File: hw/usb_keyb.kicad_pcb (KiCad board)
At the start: 2 copper layers, 99.1 x 48.3 mm, 73 parts, among them J1 POWER, J10 SPI, J12 ID, J13 ID, J2 Micro_SD_Card, J3 USB_1, J4 USB_2, J5 MX_ROW, J6 MX_COL, J7 I2C, J8 UART, J9 PROG, SW1 RESET, U1 LM3671MF, U2 STM32F407VETx, U3 STMPS2141STR, U4 STMPS2141STR, U5 74ALVC164245, U6 74ALVC164245, U7 74ALVC164245, Y1 8MHz

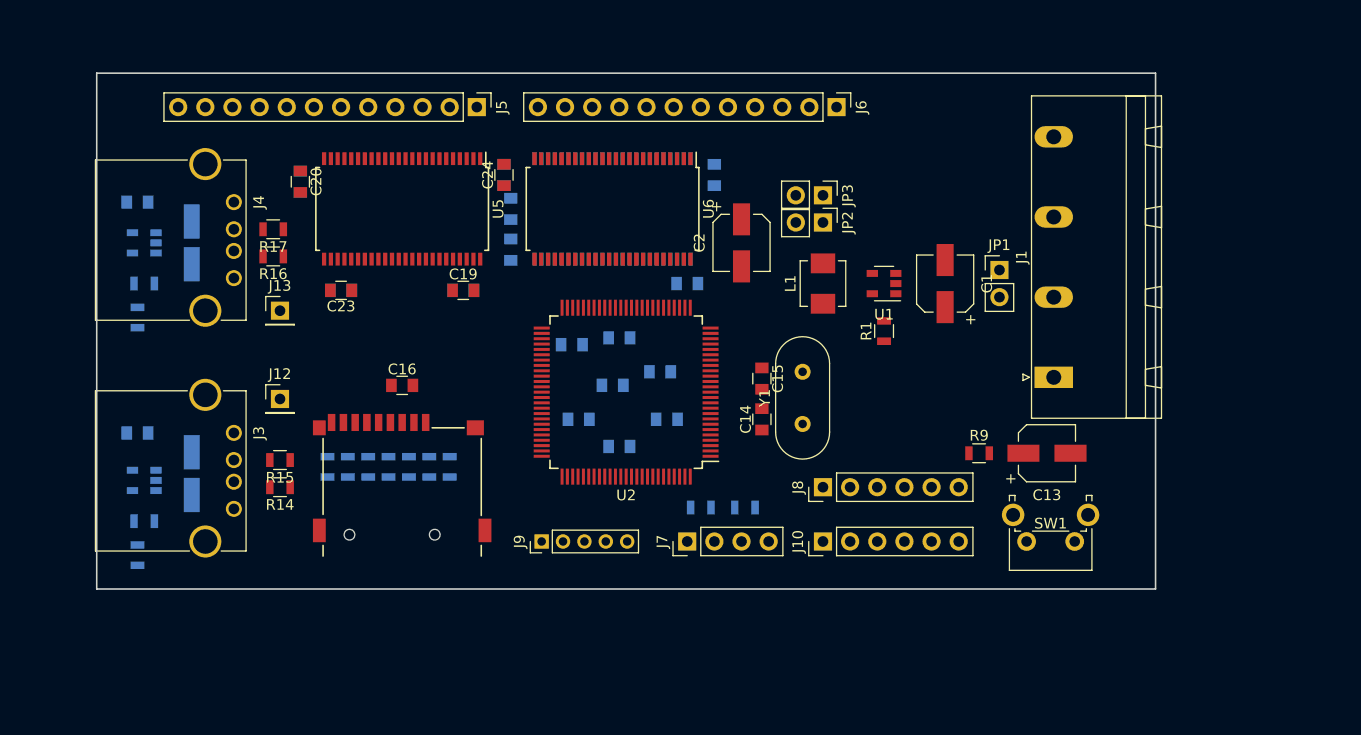
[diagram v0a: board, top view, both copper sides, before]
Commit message: Изменён разъём ZX-BUS, обновлена компоновка
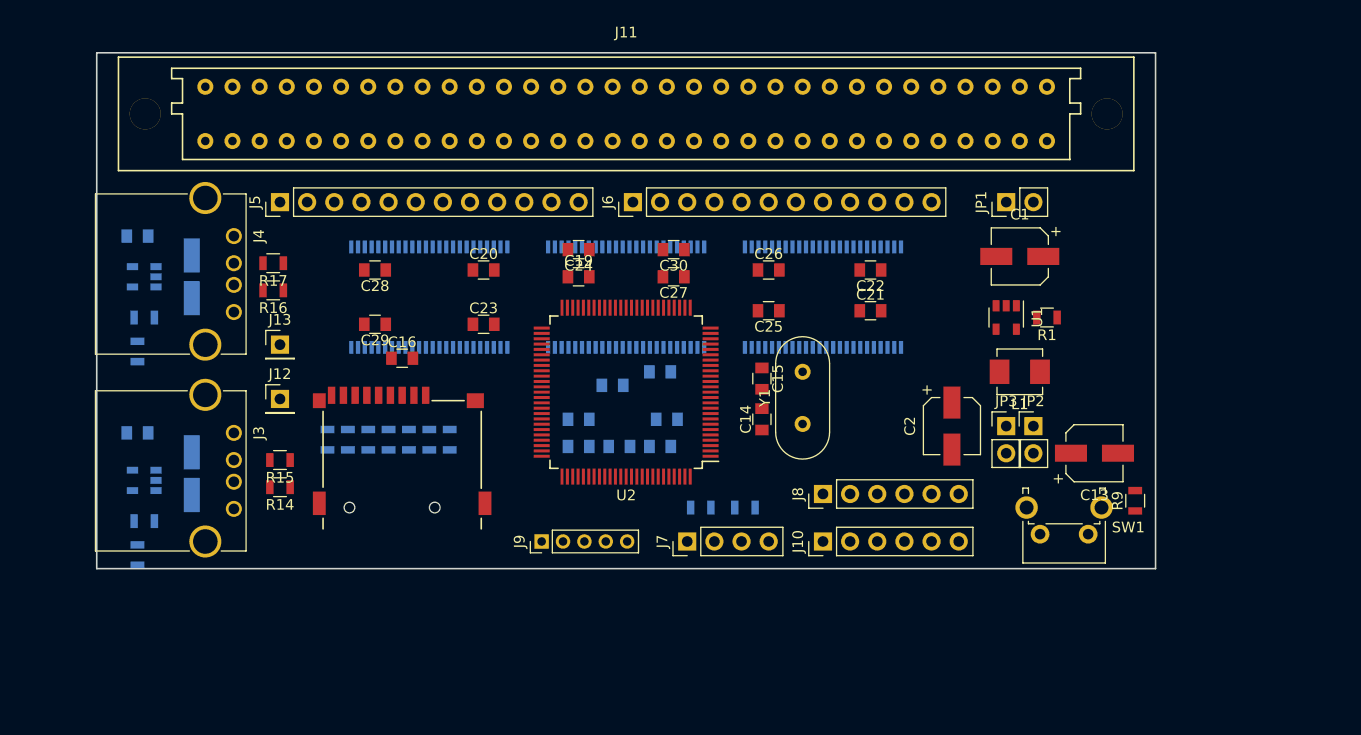
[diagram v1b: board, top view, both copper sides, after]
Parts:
- removed J1: POWER, Connectors_Phoenix:PhoenixContact_GMSTBA-G_04x7.50mm_Angled
- added J11: ZX-BUS, Connectors_IEC_DIN:Socket_DIN41612-CaseC1-AC-Female-64Pin-2rows, F.Cu at (146.1, 66.0)
- C21, C22, C25, C26, C27, C28, C29, C30: moved to F.Cu
- U5, U6: moved to B.Cu
- moved JP3 27.6 mm to (181.6, 95.2), turned to 0 degrees
- moved JP2 27.4 mm to (184.2, 95.2), turned to 0 degrees
- moved C2 26.1 mm to (176.5, 95.2)
- moved C25 24.8 mm to (159.4, 84.5), turned to 180 degrees
- moved C26 24.8 mm to (159.4, 80.6), turned to 0 degrees
- moved U6 21.3 mm to (164.5, 83.2)
- moved J6 21.0 mm to (146.7, 74.3), turned to 90 degrees
- moved J5 20.4 mm to (113.7, 74.3), turned to 90 degrees
- moved L1 20.2 mm to (182.9, 90.2), turned to 180 degrees
- moved C27 19.7 mm to (150.5, 81.3)
- moved C20 19.0 mm to (132.7, 80.6), turned to 0 degrees
- moved C30 17.3 mm to (150.5, 78.7), turned to 180 degrees
- moved C21 17.3 mm to (168.9, 84.5)
- moved C22 17.1 mm to (168.9, 80.6), turned to 180 degrees
- moved R1 15.3 mm to (185.4, 85.1), turned to 180 degrees
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
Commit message: Убраны буферные элементы, все внешние сигналы будут Open Drain
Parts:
- removed C19, C20, C21, C22, C23, C24, C25, C26, C27, C28, C29, C30: 100n, Capacitors_SMD:C_0805
- removed U5, U6, U7: 74ALVC164245, Housings_SSOP:SSOP-48_7.5x15.9mm_Pitch0.635mm
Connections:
- net DR4 renamed Net-(U2-Pad90)
- net DR5 renamed Net-(U2-Pad91)
- net DR6 renamed Net-(U2-Pad95)
- net DR7 renamed Net-(U2-Pad96)
- J2 pad 1: D2 -> D3
- J2 pad 2: D3 -> CMD
- J2 pad 3: CMD -> +3V3
- J2 pad 4: +3V3 -> CK
- J2 pad 5: CK -> GND
- J2 pad 6: GND -> D0
- J2 pad 7: D0 -> D1
- J2 pad 8: D1 -> CD
- J2 pad 9: CD -> Net-(J2-Pad9)
- U2 pad 1: O2 -> ZD2
- U2 pad 15: I0 -> ZA8
- U2 pad 16: I1 -> ZA9
- U2 pad 17: I2 -> ZA10
- U2 pad 18: I3 -> ZA11
- U2 pad 2: O3 -> ZD3
- U2 pad 23: INT0 -> ZIORQn
- U2 pad 24: INT1 -> ZRDn
- U2 pad 25: INT2 -> ZWRn
- U2 pad 26: INT3 -> ZMREQn
- U2 pad 3: O4 -> ZD4
- U2 pad 33: I4 -> ZA12
- U2 pad 34: I5 -> ZA13
- U2 pad 35: DR0 -> Net-(U2-Pad35)
- U2 pad 36: DR1 -> Net-(U2-Pad36)
- U2 pad 37: DR2 -> Net-(U2-Pad37)
- U2 pad 38: O7 -> ZD7
- U2 pad 39: O8 -> MC8
- U2 pad 4: O5 -> ZD5
- U2 pad 40: O9 -> MC9
- U2 pad 41: O10 -> MC10
- U2 pad 42: O11 -> MC11
- U2 pad 43: M1n -> ZM1n
- U2 pad 44: INTn -> ZINTn
- U2 pad 45: NMIn -> ZNMIn
- U2 pad 5: O6 -> ZD6
- U2 pad 55: A5 -> ZA5
- U2 pad 56: A6 -> ZA6
- U2 pad 57: A7 -> ZA7
- U2 pad 60: I10 -> MR10
- U2 pad 61: I11 -> MR11
- U2 pad 63: I6 -> ZA14
- U2 pad 64: I7 -> ZA15
- U2 pad 81: I8 -> MR8
- U2 pad 82: I9 -> MR9
- U2 pad 84: A0 -> ZA0
- U2 pad 85: A1 -> ZA1
- U2 pad 86: A2 -> ZA2
- U2 pad 87: A3 -> ZA3
- U2 pad 88: A4 -> ZA4
- U2 pad 89: DR3 -> Net-(U2-Pad89)
- U2 pad 97: O0 -> ZD0
- U2 pad 98: O1 -> ZD1

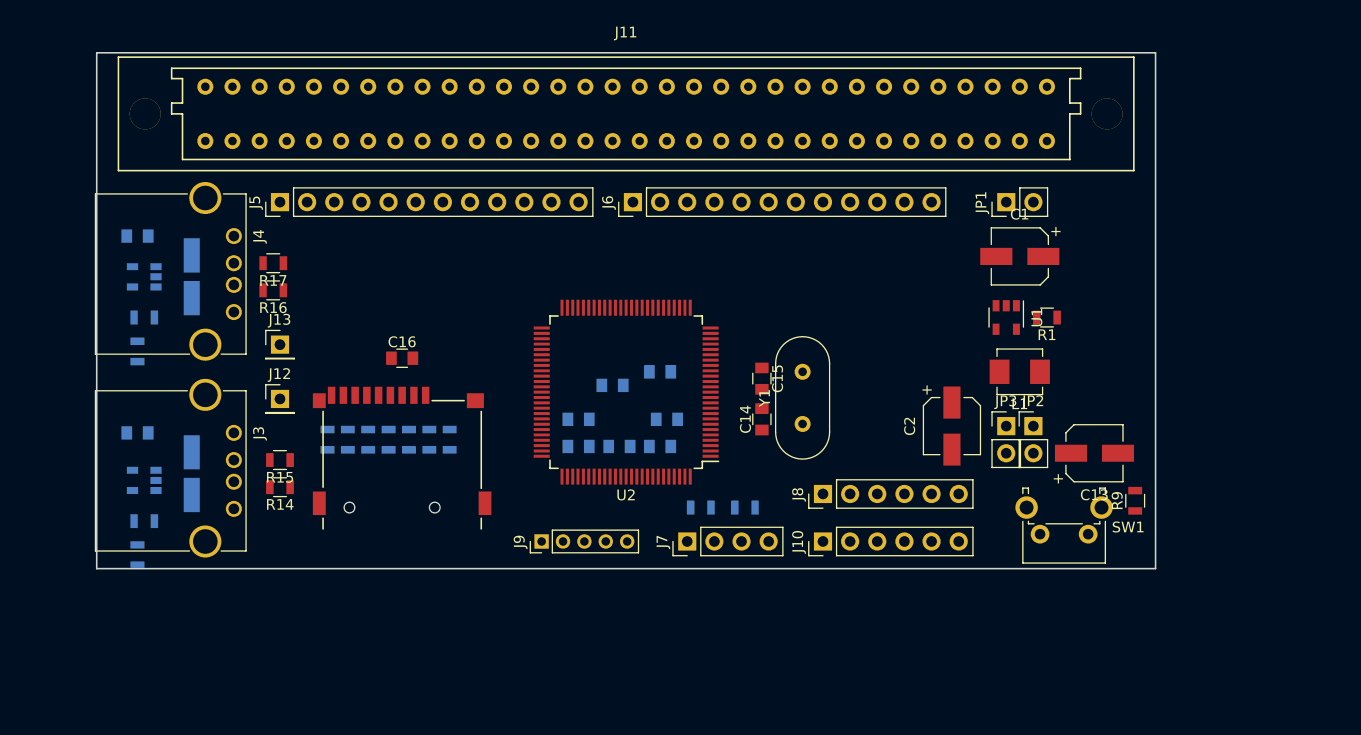
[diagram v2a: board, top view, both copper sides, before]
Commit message: Множественные изменения в схеме:
1) Заменён разъём USB на сдвоенный;
2) Добавлен Ethernet-PHY;
3) Изменено назначение служебных сигналов USB и интерфейсов;
4) внешние шины временно отключены от МК.
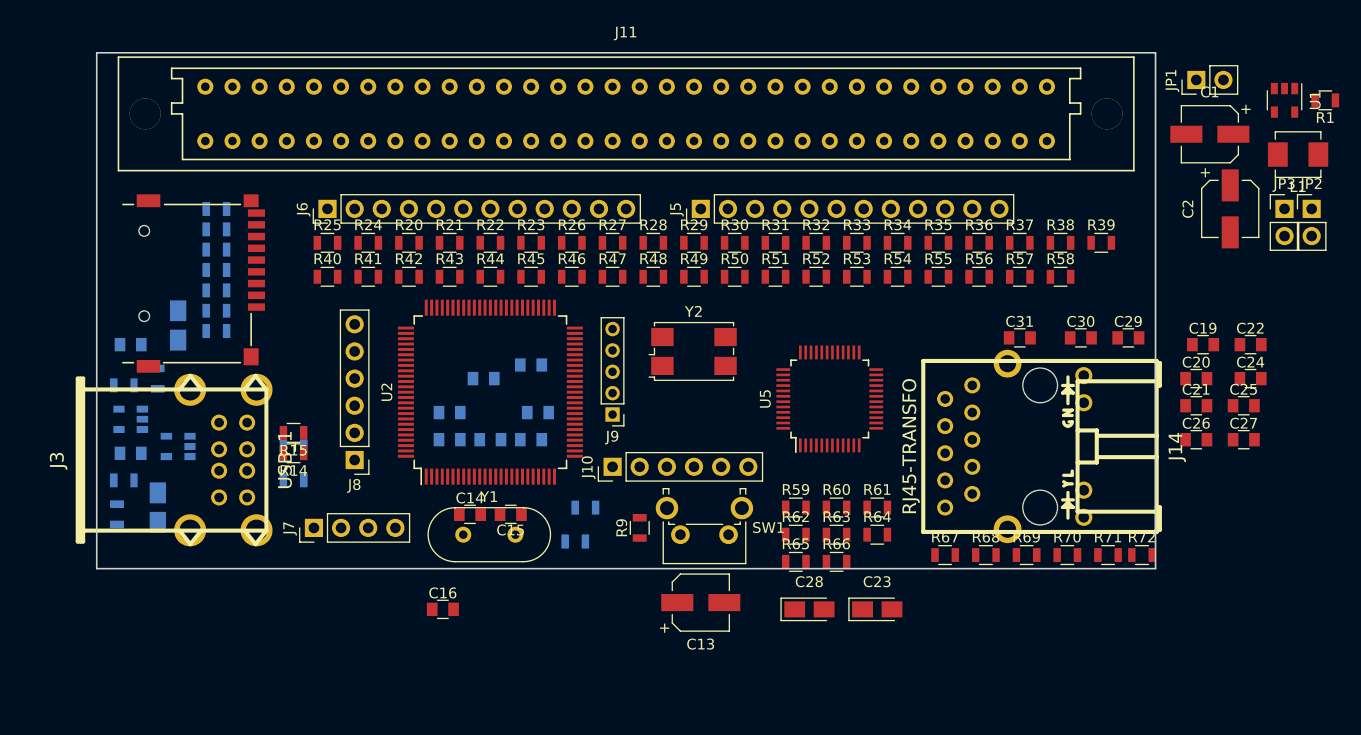
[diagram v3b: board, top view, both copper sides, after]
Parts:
- removed J12, J13: ID, Socket_Strips:Socket_Strip_Straight_1x01_Pitch2.54mm
- removed J4: USB_2, Connectors:USB_A
- added C19: 100n, Capacitors_SMD:C_0805, F.Cu at (200.0, 87.6)
- added C20: 100n, Capacitors_SMD:C_0805, F.Cu at (199.4, 90.8)
- added C21: 100n, Capacitors_SMD:C_0805, F.Cu at (199.4, 93.3)
- added C22: 100n, Capacitors_SMD:C_0805, F.Cu at (204.5, 87.6)
- added C23: 10u, Capacitors_Tantalum_SMD:CP_Tantalum_Case-A_EIA-3216-18_Reflow, F.Cu at (169.5, 112.4)
- added C24: 100n, Capacitors_SMD:C_0805, F.Cu at (204.5, 90.8)
- added C25: 100n, Capacitors_SMD:C_0805, F.Cu at (203.8, 93.3)
- added C26: 100n, Capacitors_SMD:C_0805, F.Cu at (199.4, 96.5)
- added C27: 100n, Capacitors_SMD:C_0805, F.Cu at (203.8, 96.5)
- added C28: 10u, Capacitors_Tantalum_SMD:CP_Tantalum_Case-A_EIA-3216-18_Reflow, F.Cu at (163.2, 112.4)
- added C29: 100n, Capacitors_SMD:C_0805, F.Cu at (193.0, 87.0)
- added C30: 100n, Capacitors_SMD:C_0805, F.Cu at (188.6, 87.0)
- added C31: 100n, Capacitors_SMD:C_0805, F.Cu at (182.9, 87.0)
- added J14: RJ45-TRANSFO, Projects:rj45_wurth-7499211122a, F.Cu at (184.8, 97.2)
- added R20: 10k, Resistors_SMD:R_0805, F.Cu at (125.7, 78.1)
- added R21: 10k, Resistors_SMD:R_0805, F.Cu at (129.5, 78.1)
- added R22: 10k, Resistors_SMD:R_0805, F.Cu at (133.3, 78.1)
- added R23: 10k, Resistors_SMD:R_0805, F.Cu at (137.2, 78.1)
- added R24: 10k, Resistors_SMD:R_0805, F.Cu at (121.9, 78.1)
- added R25: 10k, Resistors_SMD:R_0805, F.Cu at (118.1, 78.1)
- added R26: 10k, Resistors_SMD:R_0805, F.Cu at (141.0, 78.1)
- added R27: 10k, Resistors_SMD:R_0805, F.Cu at (144.8, 78.1)
- added R28: 10k, Resistors_SMD:R_0805, F.Cu at (148.6, 78.1)
- added R29: 10k, Resistors_SMD:R_0805, F.Cu at (152.4, 78.1)
- added R30: 10k, Resistors_SMD:R_0805, F.Cu at (156.2, 78.1)
- added R31: 10k, Resistors_SMD:R_0805, F.Cu at (160.0, 78.1)
- added R32: 10k, Resistors_SMD:R_0805, F.Cu at (163.8, 78.1)
- added R33: 10k, Resistors_SMD:R_0805, F.Cu at (167.6, 78.1)
- added R34: 10k, Resistors_SMD:R_0805, F.Cu at (171.4, 78.1)
- added R35: 10k, Resistors_SMD:R_0805, F.Cu at (175.3, 78.1)
- added R36: 10k, Resistors_SMD:R_0805, F.Cu at (179.1, 78.1)
- added R37: 10k, Resistors_SMD:R_0805, F.Cu at (182.9, 78.1)
- added R38: 10k, Resistors_SMD:R_0805, F.Cu at (186.7, 78.1)
- added R39: 10k, Resistors_SMD:R_0805, F.Cu at (190.5, 78.1)
- added R40: 10k, Resistors_SMD:R_0805, F.Cu at (118.1, 81.3)
- added R41: 10k, Resistors_SMD:R_0805, F.Cu at (121.9, 81.3)
- added R42: 10k, Resistors_SMD:R_0805, F.Cu at (125.7, 81.3)
- added R43: 10k, Resistors_SMD:R_0805, F.Cu at (129.5, 81.3)
- added R44: 10k, Resistors_SMD:R_0805, F.Cu at (133.3, 81.3)
- added R45: 10k, Resistors_SMD:R_0805, F.Cu at (137.2, 81.3)
- added R46: 10k, Resistors_SMD:R_0805, F.Cu at (141.0, 81.3)
- added R47: 10k, Resistors_SMD:R_0805, F.Cu at (144.8, 81.3)
- added R48: 10k, Resistors_SMD:R_0805, F.Cu at (148.6, 81.3)
- added R49: 10k, Resistors_SMD:R_0805, F.Cu at (152.4, 81.3)
- added R50: 10k, Resistors_SMD:R_0805, F.Cu at (156.2, 81.3)
- added R51: 10k, Resistors_SMD:R_0805, F.Cu at (160.0, 81.3)
- added R52: 10k, Resistors_SMD:R_0805, F.Cu at (163.8, 81.3)
- added R53: 10k, Resistors_SMD:R_0805, F.Cu at (167.6, 81.3)
- added R54: 10k, Resistors_SMD:R_0805, F.Cu at (171.4, 81.3)
- added R55: 10k, Resistors_SMD:R_0805, F.Cu at (175.3, 81.3)
- added R56: 10k, Resistors_SMD:R_0805, F.Cu at (179.1, 81.3)
- added R57: 10k, Resistors_SMD:R_0805, F.Cu at (182.9, 81.3)
- added R58: 10k, Resistors_SMD:R_0805, F.Cu at (186.7, 81.3)
- added R59: 2k, Resistors_SMD:R_0805, F.Cu at (161.9, 102.9)
- added R60: 2k, Resistors_SMD:R_0805, F.Cu at (165.7, 102.9)
- added R61: 10k, Resistors_SMD:R_0805, F.Cu at (169.5, 102.9)
- added R62: 2k, Resistors_SMD:R_0805, F.Cu at (161.9, 105.4)
- added R63: 2k, Resistors_SMD:R_0805, F.Cu at (165.7, 105.4)
- added R64: 4k7, Resistors_SMD:R_0805, F.Cu at (169.5, 105.4)
- added R65: 150, Resistors_SMD:R_0805, F.Cu at (161.9, 108.0)
- added R66: 18, Resistors_SMD:R_0805, F.Cu at (165.7, 108.0)
- added R67: 51, Resistors_SMD:R_0805, F.Cu at (175.9, 107.3)
- added R68: 51, Resistors_SMD:R_0805, F.Cu at (179.7, 107.3)
- added R69: 51, Resistors_SMD:R_0805, F.Cu at (183.5, 107.3)
- added R70: 51, Resistors_SMD:R_0805, F.Cu at (187.3, 107.3)
- added R71: 330, Resistors_SMD:R_0805, F.Cu at (191.1, 107.3)
- added R72: 330, Resistors_SMD:R_0805, F.Cu at (194.3, 107.3)
- added U5: DP83848C, Housings_QFP:LQFP-48_7x7mm_Pitch0.5mm, F.Cu at (165.1, 92.7)
- added Y2: 50MHz, Crystals:Crystal_SMD_7050-4pin_7.0x5.0mm, F.Cu at (152.4, 88.3)
- C17, C18: footprint Capacitors_Tantalum_SMD:CP_Tantalum_Case-A_EIA-3216-18_Hand -> Capacitors_Tantalum_SMD:CP_Tantalum_Case-A_EIA-3216-18_Reflow
- J3: footprint Connectors:USB_A -> w_conn_pc:conn_usb_Ax2
- R16, R17: moved to B.Cu
- moved R9 46.4 mm to (147.3, 104.8)
- moved J8 43.9 mm to (120.7, 98.4), turned to 180 degrees
- moved C13 39.4 mm to (153.0, 111.8)
- moved J5 39.4 mm to (153.0, 74.9)
- moved J7 34.9 mm to (116.8, 104.8)
- moved SW1 33.6 mm to (155.6, 105.4)
- moved Y1 33.4 mm to (130.8, 105.4), turned to 0 degrees
- moved R1 33.0 mm to (211.5, 64.8)
- moved L1 33.0 mm to (208.9, 69.8)
- moved U1 33.0 mm to (207.6, 64.8)
- moved C2 33.0 mm to (202.6, 74.9)
- moved JP2 33.0 mm to (210.2, 74.9)
- moved JP3 33.0 mm to (207.6, 74.9)
- moved J2 32.0 mm to (101.0, 81.9), turned to 270 degrees
- moved R7 30.7 mm to (107.7, 74.9), turned to 180 degrees
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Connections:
- net PA8 renamed Net-(U2-Pad67)
- net ZA4 renamed Net-(U2-Pad88)
- net ZA5 renamed Net-(U2-Pad55)
- net ZA6 renamed Net-(U2-Pad56)
- net ZA7 renamed Net-(U2-Pad57)
- net ZM1n renamed Net-(U2-Pad43)
- J2 pad 1: D3 -> D2
- J2 pad 2: CMD -> D3
- J2 pad 3: +3V3 -> CMD
- J2 pad 4: CK -> +3V3
- J2 pad 5: GND -> CK
- J2 pad 6: D0 -> GND
- J2 pad 7: D1 -> D0
- J2 pad 8: CD -> D1
- J2 pad 9: Net-(J2-Pad9) -> CD
- J3 pad 5: GND -> HS_VBUS
- J8 pad 1: UART3_CTS -> UART_CTS
- J8 pad 2: UART3_RTS -> UART_RTS
- J8 pad 3: UART3_TX -> UART_TX
- J8 pad 4: UART3_RX -> UART_RX
- R16 pad 2: Net-(J4-Pad3) -> Net-(J3-Pad7)
- R17 pad 2: Net-(J4-Pad2) -> Net-(J3-Pad6)
- U2 pad 1: ZD2 -> Net-(U2-Pad1)
- U2 pad 15: ZA8 -> Net-(U2-Pad15)
- U2 pad 16: ZA9 -> MDC
- U2 pad 17: ZA10 -> Net-(U2-Pad17)
- U2 pad 18: ZA11 -> Net-(U2-Pad18)
- U2 pad 2: ZD3 -> Net-(U2-Pad2)
- U2 pad 23: ZIORQn -> Net-(U2-Pad23)
- U2 pad 24: ZRDn -> ECK
- U2 pad 25: ZWRn -> MDIO
- U2 pad 26: ZMREQn -> Net-(U2-Pad26)
- U2 pad 3: ZD4 -> Net-(U2-Pad3)
- U2 pad 30: SPI_SCK -> Net-(U2-Pad30)
- U2 pad 31: SPI_MISO -> Net-(U2-Pad31)
- U2 pad 32: SPI_MOSI -> CRS
- U2 pad 33: ZA12 -> RXD0
- U2 pad 34: ZA13 -> RXD1
- U2 pad 38: ZD7 -> Net-(U2-Pad38)
- U2 pad 39: MC8 -> Net-(U2-Pad39)
- U2 pad 4: ZD5 -> Net-(U2-Pad4)
- U2 pad 40: MC9 -> Net-(U2-Pad40)
- U2 pad 41: MC10 -> Net-(U2-Pad41)
- U2 pad 42: MC11 -> Net-(U2-Pad42)
- U2 pad 44: ZINTn -> Net-(U2-Pad44)
- U2 pad 45: ZNMIn -> Net-(U2-Pad45)
- U2 pad 47: UART3_TX -> Net-(U2-Pad47)
- U2 pad 48: UART3_RX -> TX_EN
- U2 pad 5: ZD6 -> Net-(U2-Pad5)
- U2 pad 51: HS_ID -> TXD0
- U2 pad 52: HS_VBUS -> TXD1
- U2 pad 58: UART3_CTS -> Net-(U2-Pad58)
- U2 pad 59: UART3_RTS -> Net-(U2-Pad59)
- U2 pad 60: MR10 -> Net-(U2-Pad60)
- U2 pad 61: MR11 -> Net-(U2-Pad61)
- U2 pad 63: ZA14 -> Net-(U2-Pad63)
- U2 pad 64: ZA15 -> Net-(U2-Pad64)
- U2 pad 81: MR8 -> Net-(U2-Pad81)
- U2 pad 82: MR9 -> Net-(U2-Pad82)
- U2 pad 84: ZA0 -> UART_CTS
- U2 pad 85: ZA1 -> UART_RTS
- U2 pad 86: ZA2 -> UART_TX
- U2 pad 87: ZA3 -> UART_RX
- U2 pad 92: SCL -> Net-(U2-Pad92)
- U2 pad 93: SDA -> Net-(U2-Pad93)
- U2 pad 97: ZD0 -> Net-(U2-Pad97)
- U2 pad 98: ZD1 -> Net-(U2-Pad98)

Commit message: no message
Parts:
- removed J11: ZX-BUS, Connectors_IEC_DIN:Socket_DIN41612-CaseC1-AC-Female-64Pin-2rows
- added C12: 100n, Capacitors_SMD:C_0805, F.Cu at (135.3, 112.4)
- added J4: ZX-BUS, Projects:Socket_DIN41612-CaseC1-AB-Female-56Pin-2rows, F.Cu at (141.0, 66.0)
- added L2: 2.2µH, Inductors_SMD:L_0805, F.Cu at (175.3, 113.0)
- J3: footprint w_conn_pc:conn_usb_Ax2 -> Projects:conn_usb_Ax2
- moved J3 0.31 mm to (103.5, 98.1)
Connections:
- net FS_ID renamed RX
- net HS_VBUS renamed Net-(C18-Pad1)
- C17 pad 1: FS_VBUS -> Net-(C17-Pad1)
- J3 pad 1: FS_VBUS -> Net-(C17-Pad1)
- U2 pad 63: Net-(U2-Pad63) -> HS_PWR
- U2 pad 64: Net-(U2-Pad64) -> CD
- U2 pad 67: Net-(U2-Pad67) -> FS_PWR
- U2 pad 68: FS_VBUS -> TX
- U2 pad 7: CD -> Net-(U2-Pad7)
- U2 pad 8: FS_PWR -> Net-(U2-Pad8)
- U2 pad 84: UART_CTS -> Net-(U2-Pad84)
- U2 pad 85: UART_RTS -> Net-(U2-Pad85)
- U2 pad 86: UART_TX -> Net-(U2-Pad86)
- U2 pad 87: UART_RX -> Net-(U2-Pad87)
- U2 pad 9: HS_PWR -> Net-(U2-Pad9)
- U3 pad 1: FS_VBUS -> Net-(C17-Pad1)
